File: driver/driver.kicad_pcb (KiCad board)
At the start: 2 copper layers, 100 x 100 mm, 105 parts, among them J1 OUT_A, J10 FAN, J2 OUT_B, J3 UART_DEBUG, J4 USB_B_Micro, J5 CH340E module, J6 1602 I2C LCD, J7 IN_VCC, J8 IN_GND, J9 SWD, Q1 TPHR6503PL, Q2 TPHR6503PL, Q3 TPHR6503PL, Q4 TPHR6503PL, SW1 SW_Push, SW2 SW_Push, U1 MT3608, U10 PC817, U2 AMS1117-5.0, U3 AMS1117-3.3, U4 TC4427, U5 TC4427, U6 STM32F103C8Tx, U7 INA226, U8 MCP9804_MSOP, U9 PC817, Y1 8MHz

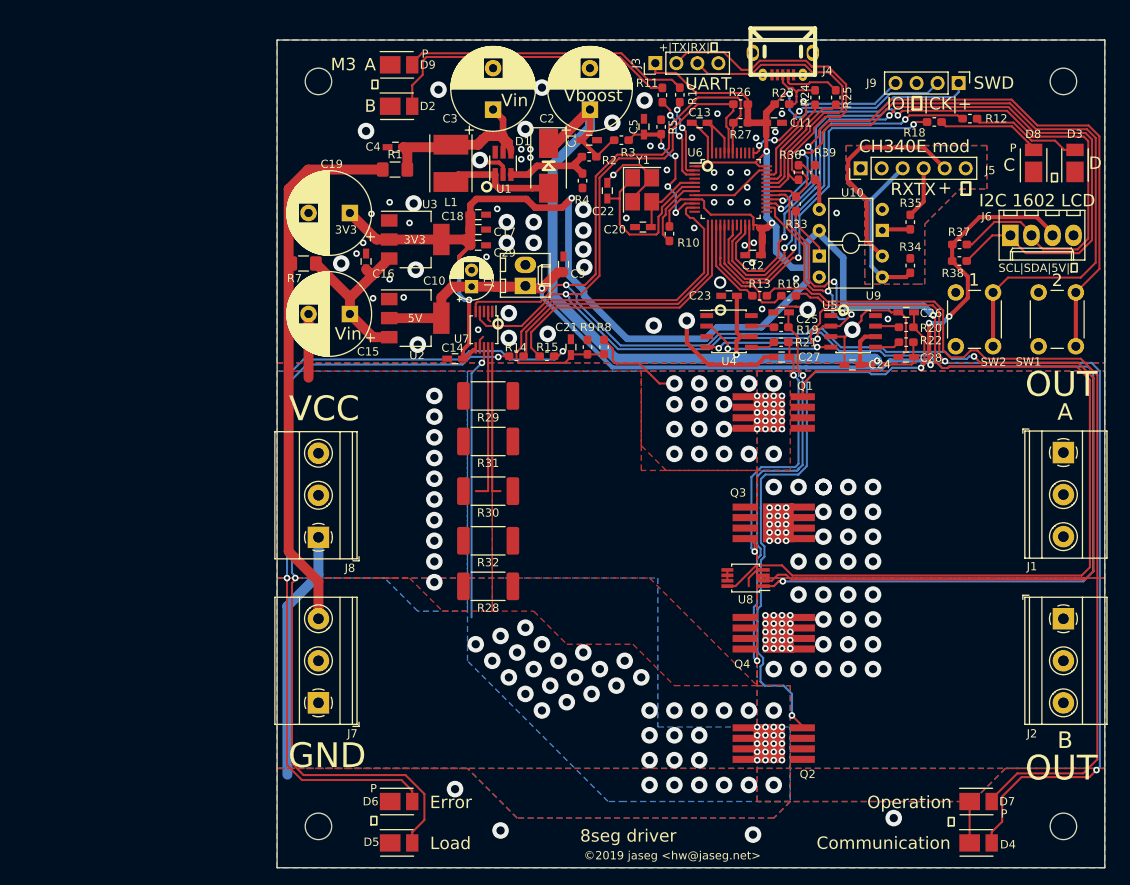
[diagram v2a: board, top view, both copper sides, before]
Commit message: driver: Add mounting holes for RS485 adapter
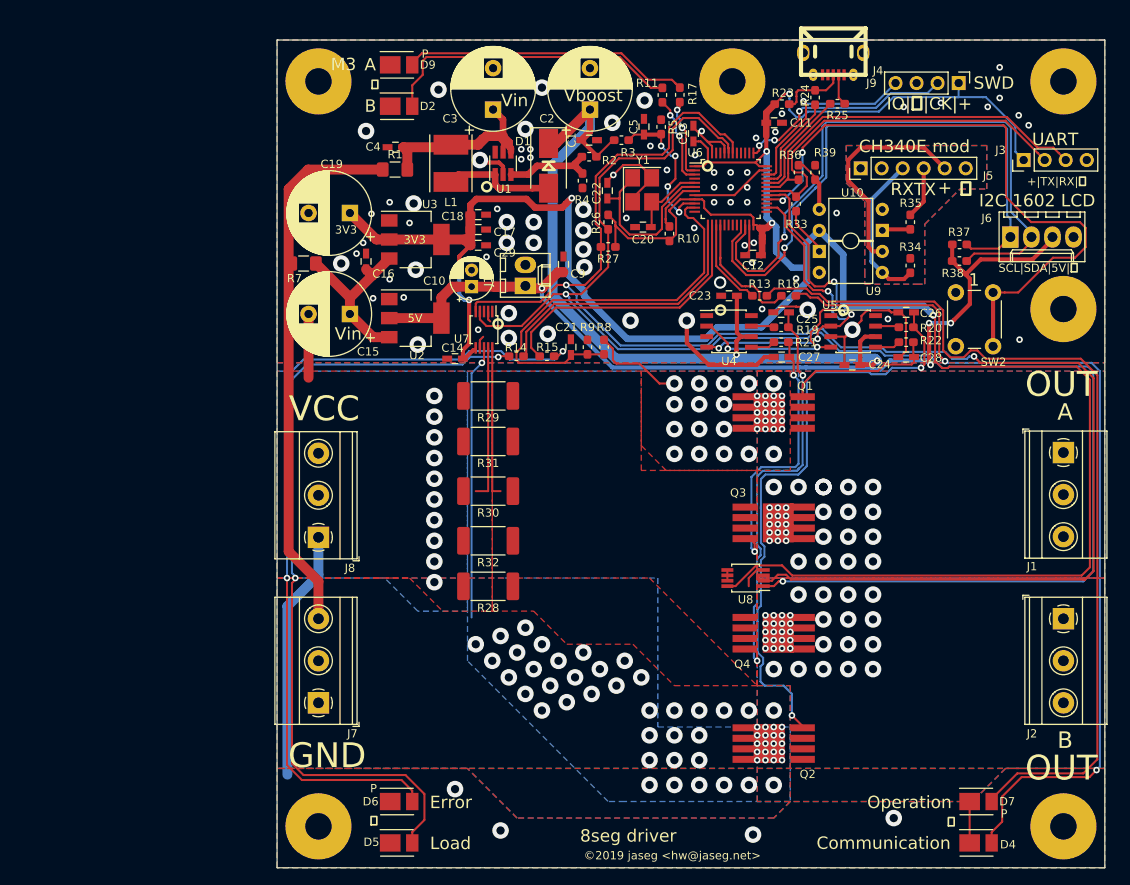
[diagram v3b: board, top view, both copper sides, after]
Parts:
- removed D3: cyan, LED_SMD:LED_PLCC_2835_Handsoldering
- removed D8: pink, LED_SMD:LED_PLCC_2835_Handsoldering
- removed R12, R18: 150, Resistor_SMD:R_0603_1608Metric_Pad1.05x0.95mm_HandSolder
- removed SW1: SW_Push, Button_Switch_THT:SW_PUSH_6mm
- added H5: MountingHole, MountingHole:MountingHole_3.2mm_M3, F.Cu at (125.0, 60.0)
- added H6: MountingHole, MountingHole:MountingHole_3.2mm_M3, F.Cu at (165.0, 87.5)
- moved J3 46.0 mm to (160.2, 69.5)
- moved R27 21.9 mm to (110.0, 80.0)
- moved R26 21.4 mm to (110.0, 77.0), turned to 270 degrees
- moved J4 6.10 mm to (137.2, 59.2)
- moved C13 1.50 mm to (120.3, 66.3), turned to 90 degrees
- moved R25 0.78 mm to (137.7, 62.7), turned to 0 degrees
- moved U9 0.56 mm to (135.5, 80.5)
- moved J6 0.20 mm to (158.6, 78.8)
- turned R10 to 270 degrees
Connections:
- R37 pad 1: /SDA_LCD -> /SCL_LCD
- R38 pad 1: /SCL_LCD -> /SDA_LCD
- U6 pad 17: /LED7 -> Net-(U6-Pad17)
- U6 pad 19: /LED1 -> Net-(U6-Pad19)
- U6 pad 27: /SW0 -> Net-(U6-Pad27)
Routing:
- net /SW0: track 77.7 -> 0.00 mm, vias 2 -> 0
- net /LED1: track 48.7 -> 0.00 mm, vias 2 -> 0
- net /LED7: track 44.9 -> 0.00 mm, vias 2 -> 0
- net /SCL_LCD: track 96.1 -> 72.0 mm, vias 2 -> 1
- net /SDA_LCD: track 95.2 -> 76.9 mm, vias 2 -> 1
- net Net-(D3-Pad2): track 13.3 -> 0.00 mm
- net Net-(D8-Pad2): track 12.7 -> 0.00 mm
- net /SW1: track 85.4 -> 77.1 mm
- net +3V3: track 329.1 -> 336.4 mm
- net /UART_RX: track 39.1 -> 45.1 mm
- net /SCL_INA: track 193.7 -> 188.4 mm
- net /SDA_INA: track 192.8 -> 188.9 mm
- net Net-(J4-Pad2): track 7.25 -> 3.80 mm
- net Net-(R10-Pad1): track 8.73 -> 6.87 mm
- net /UART_TX: track 46.6 -> 45.0 mm
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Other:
- board text removed: "2"
- board text removed: "C"
- board text removed: "D"

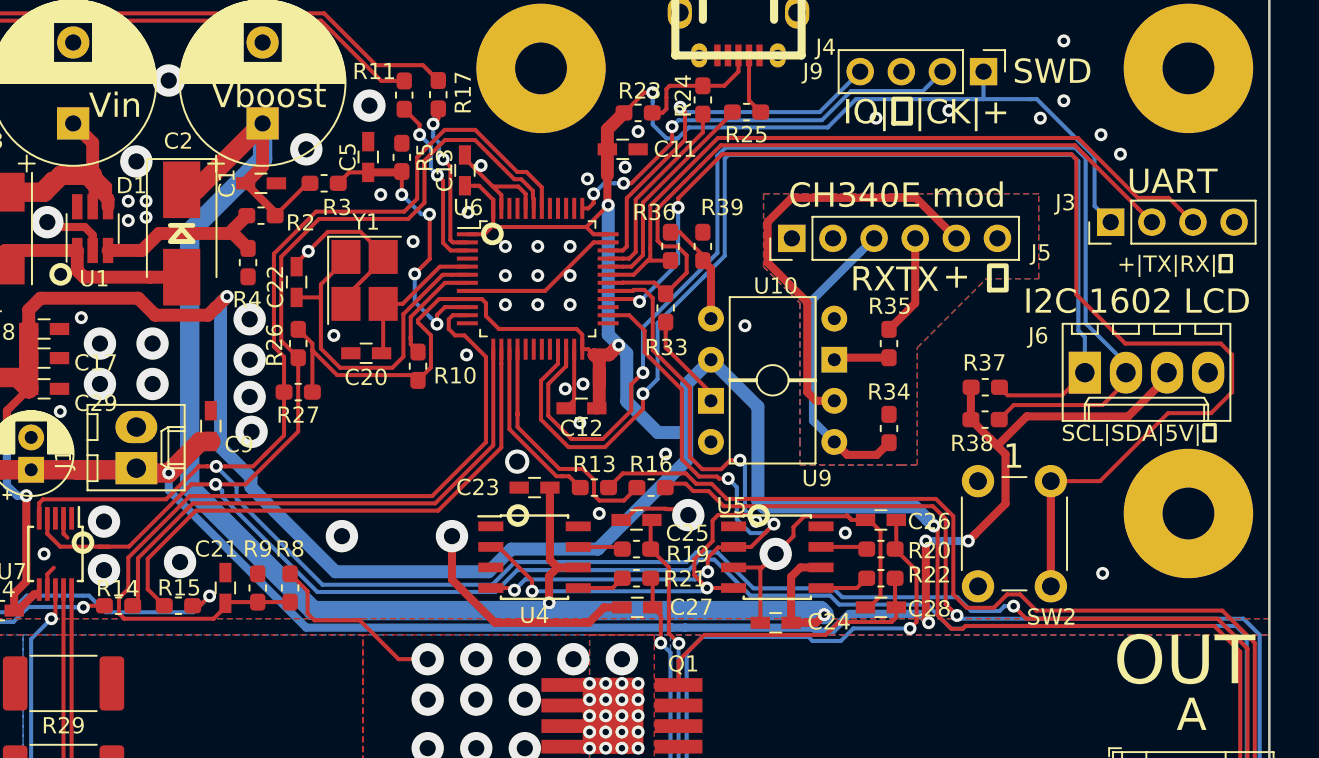
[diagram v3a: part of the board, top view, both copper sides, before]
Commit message: Fix lcd connector position
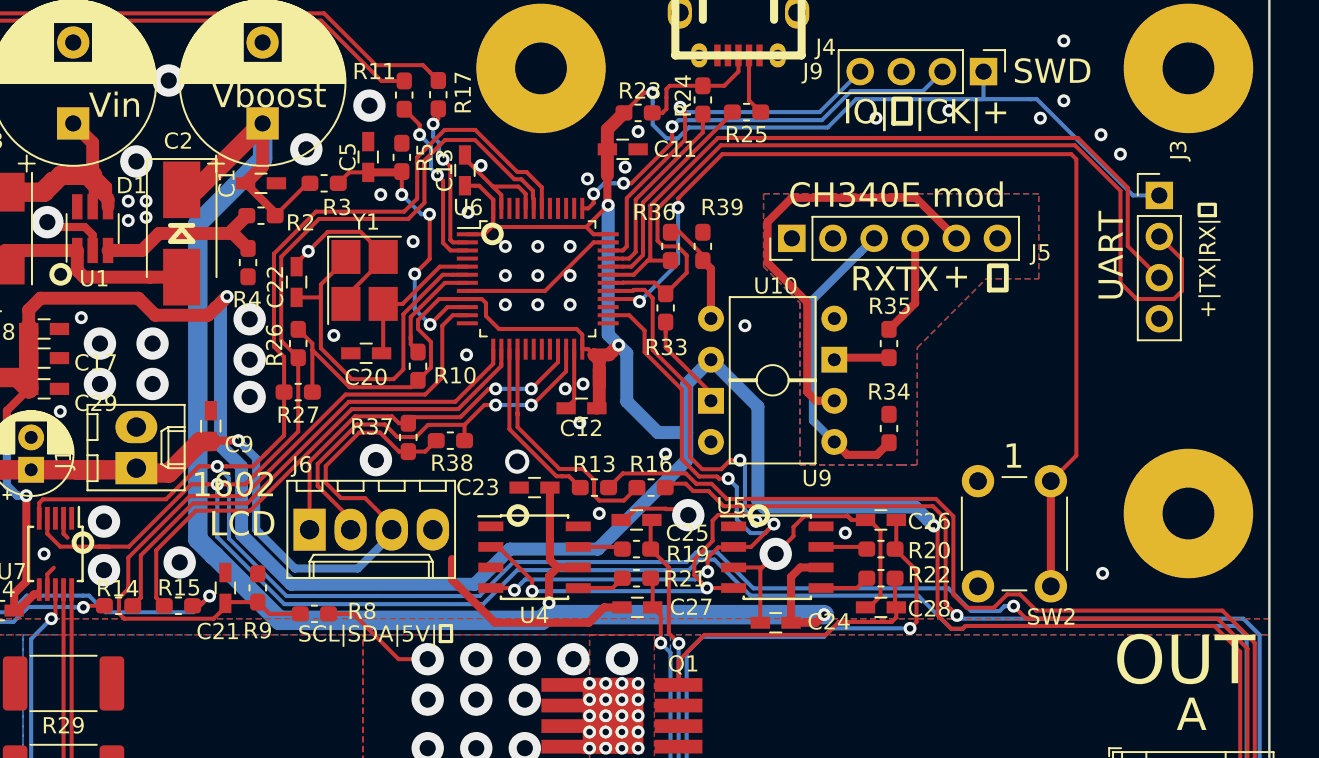
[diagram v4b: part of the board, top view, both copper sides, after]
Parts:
- moved J6 48.9 mm to (110.7, 88.5)
- moved R37 35.8 mm to (116.8, 82.8), turned to 270 degrees
- moved R38 33.1 mm to (119.4, 83.0)
- moved J3 3.42 mm to (163.2, 67.8), turned to 0 degrees
- moved R8 2.19 mm to (111.0, 93.7), turned to 180 degrees
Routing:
- net /SDA_LCD: track 76.9 -> 25.6 mm, vias 1 -> 2
- net +5V: track 115.6 -> 64.7 mm, vias 4 -> 1
- net /SCL_LCD: track 72.0 -> 23.2 mm, vias 1 -> 2
- net /SW1: track 77.1 -> 62.3 mm
- net /UART_TX: track 45.0 -> 56.3 mm
- net /VIN_MON: track 50.1 -> 44.9 mm
- net +3V3: track 336.4 -> 340.6 mm
- net /VIN: track 110.4 -> 106.2 mm
- net /LED4: track 34.1 -> 30.7 mm
- net /LED3: track 33.8 -> 30.9 mm
- net /SCL_INA: track 188.4 -> 190.7 mm
- net +VSW: track 99.4 -> 101.6 mm
- net /SDA_INA: track 188.9 -> 191.1 mm
- net /UART_RX: track 45.1 -> 46.6 mm
- net GND: track 140.8 -> 139.4 mm, vias 90 -> 88
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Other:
- board text added: "1602 LCD"
- board text removed: "I2C 1602 LCD"

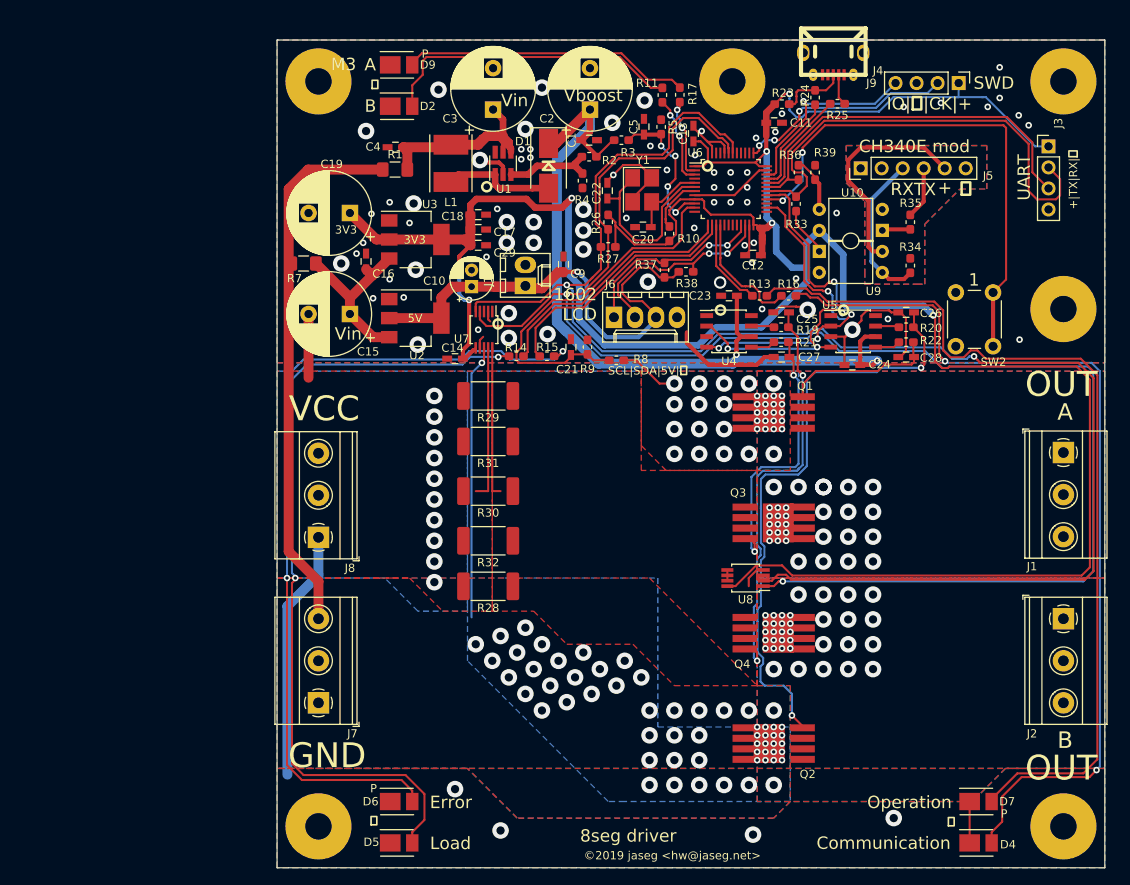
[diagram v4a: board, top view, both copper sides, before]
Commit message: Throw out a bunch, use a different microcontroller
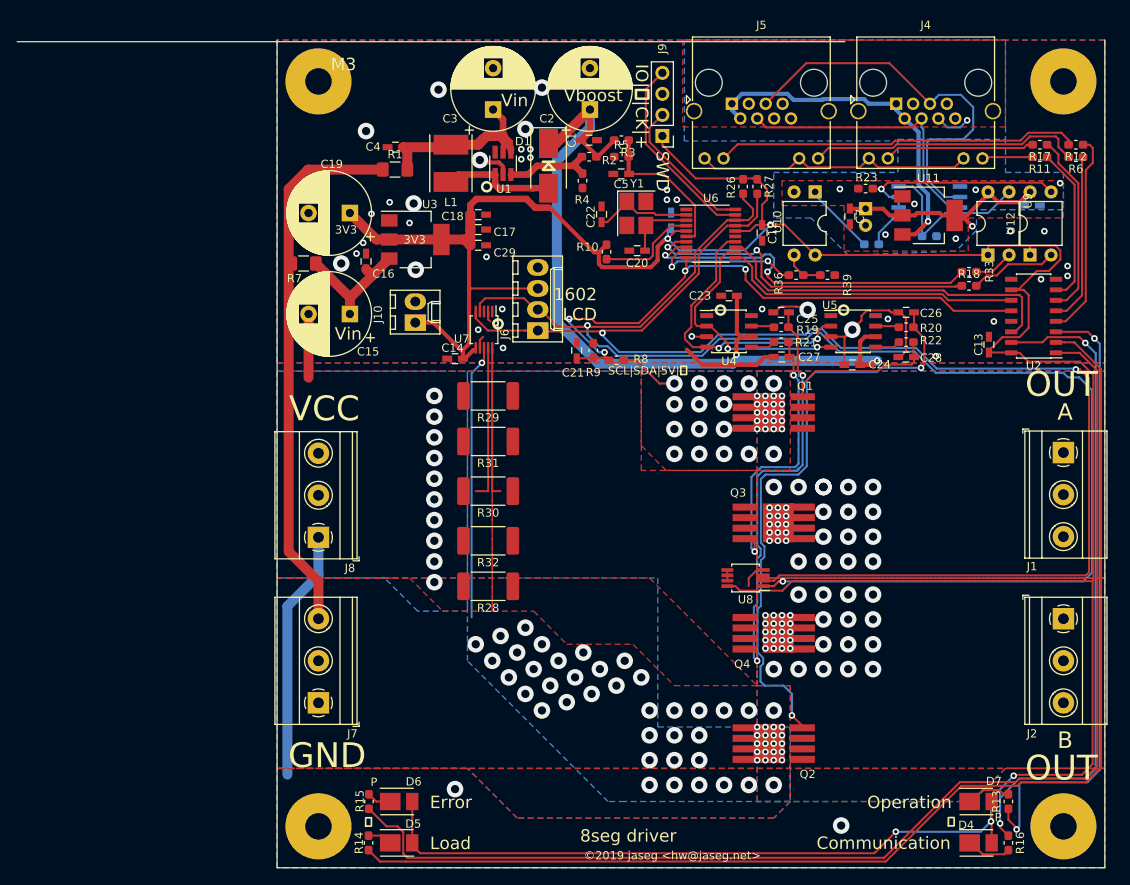
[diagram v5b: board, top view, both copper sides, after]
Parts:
- removed C10: 22u, Capacitor_THT:CP_Radial_D5.0mm_P2.00mm
- removed C9: 10u, Capacitors_SMD:C_0603_HandSoldering
- removed D2: cyan, LED_SMD:LED_PLCC_2835_Handsoldering
- removed D9: pink, LED_SMD:LED_PLCC_2835_Handsoldering
- removed H5, H6: MountingHole, MountingHole:MountingHole_3.2mm_M3
- removed J3: UART_DEBUG, Pin_Headers:Pin_Header_Straight_1x04_Pitch2.54mm
- removed R24, R25: 22, Resistor_SMD:R_0603_1608Metric_Pad1.05x0.95mm_HandSolder
- removed R37, R38: 1k5, Resistor_SMD:R_0603_1608Metric_Pad1.05x0.95mm_HandSolder
- removed SW2: SW_Push, Button_Switch_THT:SW_PUSH_6mm
- added C6: 100n, Capacitors_SMD:C_0603_HandSoldering, B.Cu at (161.2, 75.0)
- added C7: 10u, Capacitors_SMD:C_0603_HandSoldering, F.Cu at (139.2, 76.3)
- added C8: 22u, Capacitor_THT:CP_Radial_D5.0mm_P2.00mm, B.Cu at (141.1, 75.4)
- added R12: 150, Resistor_SMD:R_0603_1608Metric_Pad1.05x0.95mm_HandSolder, F.Cu at (166.5, 67.7)
- added R18: 390, Resistor_SMD:R_0603_1608Metric_Pad1.05x0.95mm_HandSolder, F.Cu at (153.6, 84.7)
- added R6: 150, Resistor_SMD:R_0603_1608Metric_Pad1.05x0.95mm_HandSolder, F.Cu at (166.5, 69.2)
- added U11: AMS1117-5.0, Package_TO_SOT_SMD:SOT-223-3_TabPin2, F.Cu at (148.7, 76.2)
- added U12: PC817, Package_DIP:DIP-4_W7.62mm, F.Cu at (161.0, 81.0)
- added U13: MAX485E, Package_SO:SO-8_5.3x6.2mm_P1.27mm, B.Cu at (148.8, 74.6)
- C11, R34, R35: moved to B.Cu
- J4: value USB_B_Micro -> RJ45_LED_Shielded; footprint footprints:microusb_ali_dovetail -> Connector_RJ:RJ45_Amphenol_RJHSE538X
- J5: value CH340E module -> RJ45_LED_Shielded; footprint Pin_Headers:Pin_Header_Straight_1x06_Pitch2.54mm -> Connector_RJ:RJ45_Amphenol_RJHSE538X
- R23: value 1k5 -> 720
- U2: value AMS1117-5.0 -> 74HC595; footprint Package_TO_SOT_SMD:SOT-223-3_TabPin2 -> Package_SO:SOIC-16_3.9x9.9mm_P1.27mm
- U6: value STM32F103C8Tx -> STM32F030F4Px; footprint Package_QFP:LQFP-48_7x7mm_P0.5mm -> Package_SO:TSSOP-20_4.4x6.5mm_P0.65mm
- moved U2 74.7 mm to (161.4, 88.3), turned to 180 degrees
- moved R16 71.2 mm to (158.3, 152.0), turned to 270 degrees
- moved R13 68.1 mm to (158.3, 147.0), turned to 90 degrees
- moved R14 61.4 mm to (81.0, 152.0), turned to 90 degrees
- moved R15 57.9 mm to (81.1, 147.0), turned to 90 degrees
- moved R11 46.2 mm to (162.2, 69.2), turned to 180 degrees
- moved R17 43.9 mm to (162.2, 67.7), turned to 180 degrees
- moved C13 43.9 mm to (156.0, 91.8)
- moved J9 36.4 mm to (116.5, 66.6), turned to 180 degrees
- moved R33 22.5 mm to (153.6, 83.0), turned to 0 degrees
- moved U9 20.4 mm to (155.9, 81.0), turned to 90 degrees
- moved R27 19.4 mm to (128.0, 72.7), turned to 270 degrees
- moved J5 17.4 mm to (125.0, 62.7), turned to 0 degrees
- moved C11 17.2 mm to (117.6, 76.8), turned to 90 degrees
- moved R26 16.9 mm to (126.3, 72.7)
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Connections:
- C20 pad 2: Net-(C20-Pad2) -> /XT1
- C22 pad 1: Net-(C22-Pad1) -> /XT2
- D4 pad 1: GND -> Net-(D4-Pad1)
- D4 pad 2: Net-(D4-Pad2) -> +3V3
- D5 pad 1: GND -> Net-(D5-Pad1)
- D5 pad 2: Net-(D5-Pad2) -> +3V3
- D6 pad 1: GND -> Net-(D6-Pad1)
- D6 pad 2: Net-(D6-Pad2) -> +3V3
- D7 pad 1: GND -> Net-(D7-Pad1)
- D7 pad 2: Net-(D7-Pad2) -> +3V3
- J10 pad 1: +5V -> +3V3
- J4 pad 1: Net-(J4-Pad1) -> /BUS_VCC
- J4 pad 2: Net-(J4-Pad2) -> /BUS_VCC
- J4 pad 3: Net-(J4-Pad3) -> /ISO_GND
- J4 pad 4: Net-(J4-Pad4) -> /RS485_B
- J4 pad 5: GND -> /RX485_A
- J4 pad 6: GND -> /ISO_GND
- J5 pad 1: Net-(J5-Pad1) -> /BUS_VCC
- J5 pad 2: Net-(J5-Pad2) -> /BUS_VCC
- J5 pad 3: Net-(J5-Pad3) -> /ISO_GND
- J5 pad 4: Net-(J5-Pad4) -> /RS485_B
- J5 pad 5: /ISO_5V -> /RX485_A
- J6 pad 1: /SCL_LCD -> /SCL
- J6 pad 2: /SDA_LCD -> /SDA
- J6 pad 3: +5V -> +3V3
- R10 pad 1: Net-(R10-Pad1) -> /RST
- R11 pad 1: /LED0 -> Net-(R11-Pad1)
- R11 pad 2: Net-(D2-Pad2) -> /CLED1
- R13 pad 1: /LED2 -> /SLED1
- R13 pad 2: Net-(D7-Pad2) -> Net-(D7-Pad1)
- R14 pad 1: /LED3 -> /SLED2
- R14 pad 2: Net-(D5-Pad2) -> Net-(D5-Pad1)
- R15 pad 1: /LED4 -> /SLED3
- R15 pad 2: Net-(D6-Pad2) -> Net-(D6-Pad1)
- R16 pad 1: /LED5 -> /SLED4
- R16 pad 2: Net-(D4-Pad2) -> Net-(D4-Pad1)
- R17 pad 1: /LED6 -> Net-(R17-Pad1)
- R17 pad 2: Net-(D9-Pad2) -> /CLED2
- R23 pad 1: Net-(J4-Pad3) -> /ISO_DE
- R23 pad 2: +3V3 -> /ISO_GND
- R26 pad 2: /SDA_INA -> /SDA
- R27 pad 2: /SCL_INA -> /SCL
- R33 pad 1: /UART_TX -> /TX
- R34 pad 1: Net-(J5-Pad3) -> /ISO_DI
- R35 pad 1: Net-(R35-Pad1) -> /ISO_RO
- R35 pad 2: Net-(J5-Pad4) -> Net-(R35-Pad2)
- R36 pad 1: Net-(R36-Pad1) -> /RX
- R36 pad 2: /UART_RX -> Net-(R36-Pad2)
- R39 pad 2: Net-(R36-Pad1) -> Net-(R36-Pad2)
- U10 pad 1: Net-(R35-Pad1) -> Net-(R35-Pad2)
- U10 pad 3: Net-(R36-Pad1) -> Net-(R36-Pad2)
- U2 pad 1: GND -> /SLED3
- U2 pad 2: +5V -> /SLED2
- U2 pad 3: Net-(C15-Pad1) -> /SLED1
- U6 pad 1: +3V3 -> GND
- U6 pad 10: /VBOOT_MON -> /VIN_MON
- U6 pad 11: /VIN_MON -> /SCK
- U6 pad 12: Net-(U6-Pad12) -> /CTRL_A
- U6 pad 13: /LED3 -> /MOSI
- U6 pad 14: /LED4 -> /CTRL_B
- U6 pad 15: /LED2 -> GND
- U6 pad 16: /LED5 -> +3V3
- U6 pad 17: Net-(U6-Pad17) -> /SCL
- U6 pad 18: Net-(U6-Pad18) -> /SDA
- U6 pad 19: Net-(U6-Pad19) -> /SWDIO
- U6 pad 2: /LED6 -> /XT2
- U6 pad 20: Net-(U6-Pad20) -> /SWCLK
- U6 pad 3: /LED0 -> /XT1
- U6 pad 4: Net-(U6-Pad4) -> /RST
- U6 pad 5: Net-(C20-Pad2) -> +3V3
- U6 pad 6: Net-(C22-Pad1) -> /VBOOT_MON
- U6 pad 7: Net-(R10-Pad1) -> /DE
- U6 pad 8: GND -> /TX
- U6 pad 9: +3V3 -> /RX
- U7 pad 4: /SDA_INA -> /SDA
- U7 pad 5: /SCL_INA -> /SCL
- U8 pad 1: /SDA_INA -> /SDA
- U8 pad 2: /SCL_INA -> /SCL
- U9 pad 1: Net-(R33-Pad2) -> +3V3
- U9 pad 2: GND -> Net-(R33-Pad2)
- U9 pad 3: Net-(J5-Pad3) -> /ISO_DI
- Y1 pad 1: Net-(C22-Pad1) -> /XT2
- Y1 pad 3: Net-(C20-Pad2) -> /XT1
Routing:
- net /SDA_INA: track 191.1 -> 0.00 mm, vias 2 -> 0
- net /SCL_INA: track 190.7 -> 0.00 mm, vias 2 -> 0
- net /SDA: track 0.00 -> 176.6 mm, vias 0 -> 2
- net /SCL: track 0.00 -> 172.4 mm, vias 0 -> 2
- net /SLED3: track 0.00 -> 150.2 mm
- net /SLED2: track 0.00 -> 148.7 mm
- net Net-(D4-Pad2): track 111.0 -> 0.00 mm, vias 2 -> 0
- net Net-(D7-Pad2): track 109.6 -> 0.00 mm
- net Net-(D6-Pad2): track 101.4 -> 0.00 mm, vias 2 -> 0
- net Net-(D5-Pad2): track 98.2 -> 0.00 mm, vias 2 -> 0
- net /SLED4: track 0.00 -> 79.5 mm, vias 0 -> 2
- net /SLED1: track 0.00 -> 76.4 mm, vias 0 -> 2
- net +5V: track 64.7 -> 0.00 mm, vias 1 -> 0
- net /SW1: track 62.3 -> 0.00 mm, vias 2 -> 0
- net /UART_TX: track 56.3 -> 0.00 mm
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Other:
- board size 100 x 100 mm -> 131.4 x 100 mm
- board text removed: "+"
- board text removed: "+|TX|RX|⏚"
- board text removed: "1"
- board text removed: "5V"
- board text removed: "CH340E mod"
- board text removed: "RX"
- board text removed: "TX"
- board text removed: "UART"
